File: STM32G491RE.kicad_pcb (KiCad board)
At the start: 2 copper layers, 210.5 x 121.5 mm, 147 parts, among them J4 OLED I2C, J5 BAT VIN, J6 TYPE-C_16PIN_2MD__073_, J7 Battery, Q1 PMOS, Q2 PMOS, Q3 PMOS, U1 TPS564257DRLR, U10 ESP32-S3-MINI-1-N8, U2 STM32G491RETx, U3 TPS2113ADRBR, U4 DRV8835DSSR, U5 M24M02-DRMN6TP, U6 MP2639A, U7 TPS79601DRBR, U8 LMV331M5, U9 LMV331M5, Y1 24MHz, Y2 32.768KHz

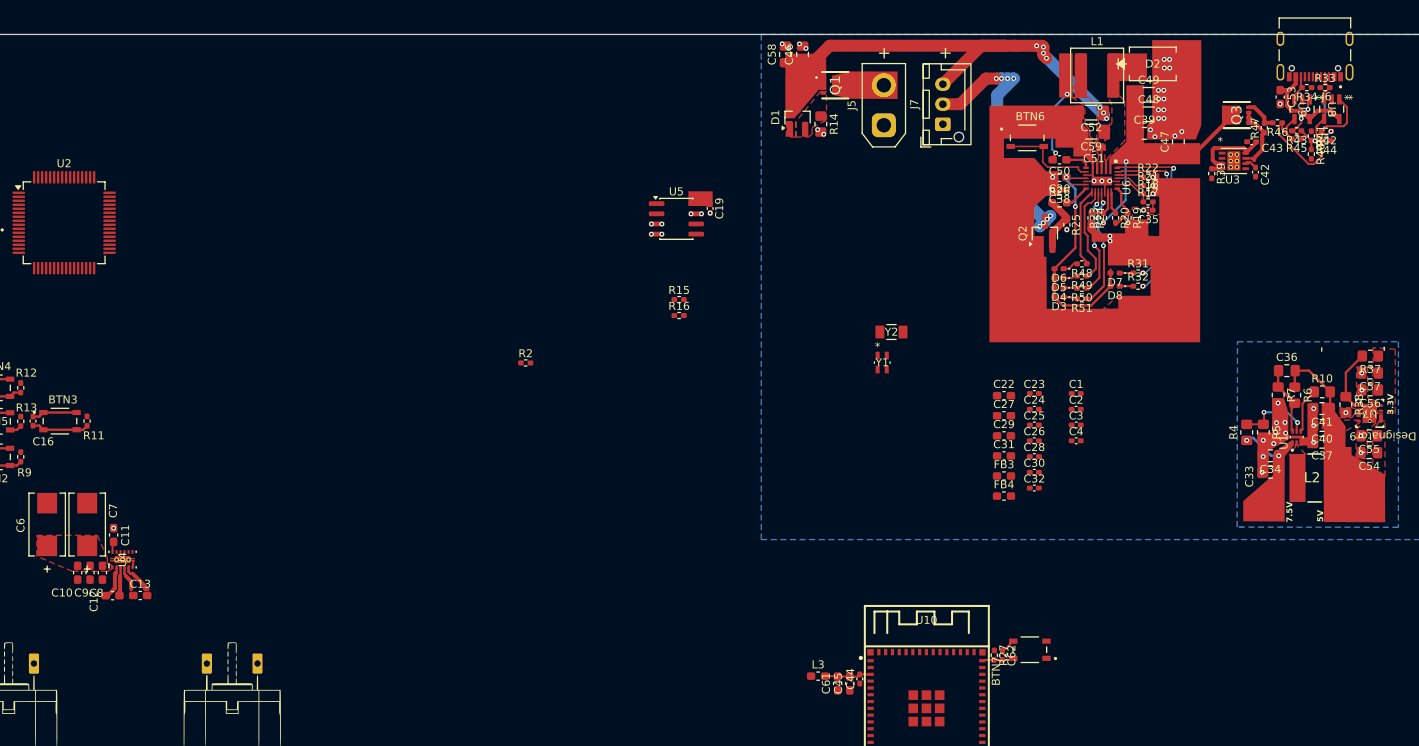
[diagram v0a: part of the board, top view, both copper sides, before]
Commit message: changed most of the components to 0805
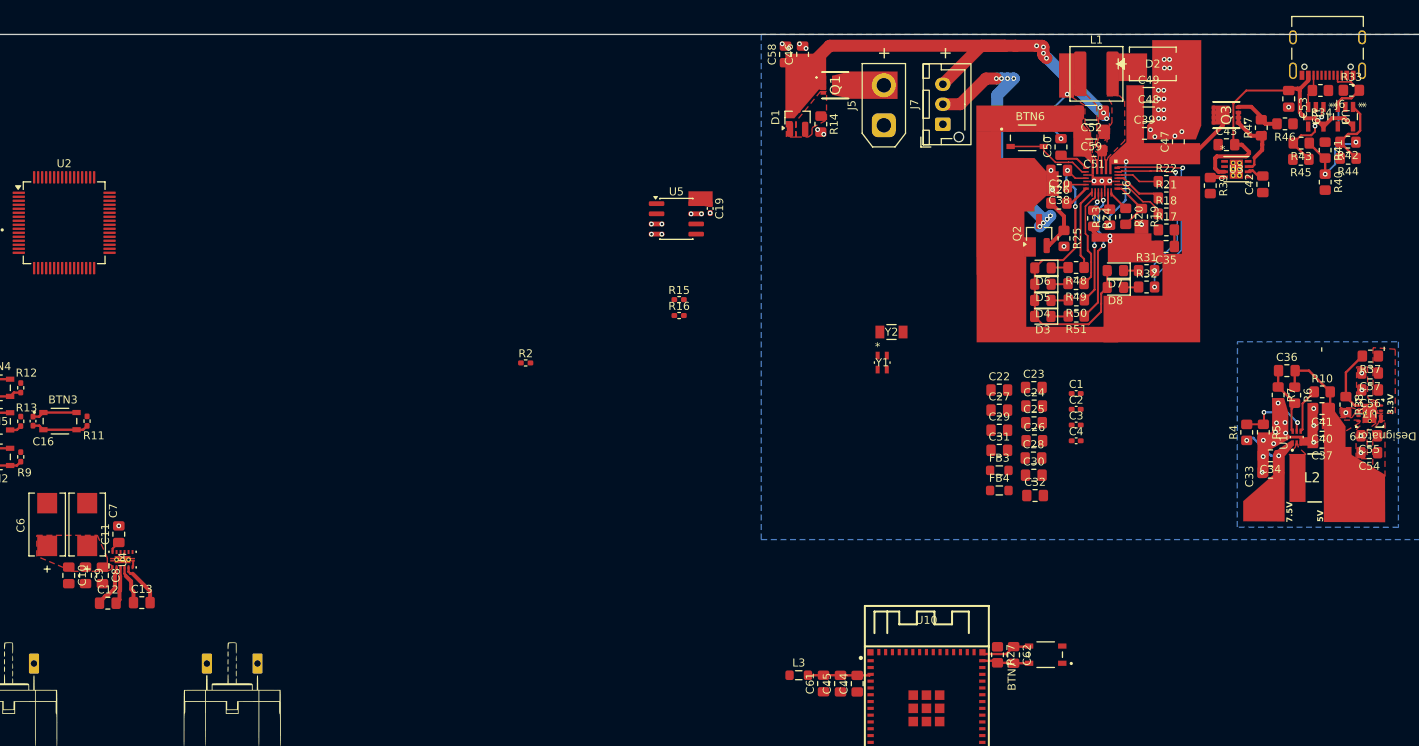
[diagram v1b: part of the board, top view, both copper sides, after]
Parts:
- C10, C11, C12, C13, C20, C22, C27, C29, C31, C45, C50, C51, C53, C61, C8, C9: footprint Capacitor_SMD:C_0603_1608Metric_Pad1.08x0.95mm_HandSolder -> Capacitor_SMD:C_0805_2012Metric_Pad1.18x1.45mm_HandSolder
- C23, C24, C25, C26, C28, C30, C32, C35, C38, C42, C43, C44, C62: footprint Capacitor_SMD:C_0402_1005Metric_Pad0.74x0.62mm_HandSolder -> Capacitor_SMD:C_0805_2012Metric_Pad1.18x1.45mm_HandSolder
- D3, D4, D5, D6, D7, D8: footprint LED_SMD:LED_0402_1005Metric_Pad0.77x0.64mm_HandSolder -> LED_SMD:LED_0805_2012Metric_Pad1.15x1.40mm_HandSolder
- FB3, FB4, L3: footprint Inductor_SMD:L_0603_1608Metric_Pad1.05x0.95mm_HandSolder -> Inductor_SMD:L_0805_2012Metric_Pad1.05x1.20mm_HandSolder
- R17, R18, R19, R20, R21, R22, R23, R24, R25, R27, R31, R32, R33, R34, R39, R40, R41, R42, R43, R44, R45, R46, R47, R48, R49, R50, R51: footprint Resistor_SMD:R_0402_1005Metric_Pad0.72x0.64mm_HandSolder -> Resistor_SMD:R_0805_2012Metric_Pad1.20x1.40mm_HandSolder
- R26: footprint Resistor_SMD:R_0603_1608Metric_Pad0.98x0.95mm_HandSolder -> Resistor_SMD:R_0805_2012Metric_Pad1.20x1.40mm_HandSolder
- moved C35 5.06 mm to (192.7, 39.9)
- moved R17 4.18 mm to (192.8, 37.9)
- moved R40 3.91 mm to (212.6, 31.9)
- moved R44 3.50 mm to (215.5, 28.9)
- moved R18 3.40 mm to (192.8, 35.9)
- moved R33 3.31 mm to (215.9, 20.4)
- moved C43 3.17 mm to (200.3, 27.2)
- moved D3 3.16 mm to (177.3, 48.7)
- moved R42 3.03 mm to (215.5, 26.9)
- moved R21 2.75 mm to (192.8, 33.9)
- moved R45 2.62 mm to (209.6, 29.0)
- moved D4 2.57 mm to (177.3, 46.7)
- moved R41 2.47 mm to (212.6, 27.9)
- moved L3 2.42 mm to (146.8, 93.5)
- moved R22 2.34 mm to (192.8, 31.8)
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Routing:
- net Net-(R44-Pad2): track 19.9 -> 0.00 mm
- net +5V_USBC: track 22.6 -> 36.7 mm
- net +VCC: track 29.5 -> 40.4 mm
- net +VREF_COMP: track 7.01 -> 12.6 mm
- net CC1: track 3.38 -> 7.85 mm
- net GND: track 5.02 -> 8.87 mm, vias 61 -> 57
- net Net-(R43-Pad2): track 6.57 -> 9.64 mm
- net Net-(U6-SW): track 12.4 -> 9.84 mm
- net Net-(U6-ISET): track 3.65 -> 6.16 mm
- net Net-(U6-LED4): track 15.1 -> 17.5 mm
- net Net-(U6-IB): track 4.76 -> 6.94 mm
- net Net-(U10-3V3): track 5.82 -> 7.90 mm
- net Net-(U6-ILIM): track 3.48 -> 5.48 mm
- net ESP_EN: track 3.99 -> 5.98 mm
- net BOUT1: track 3.08 -> 4.89 mm
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
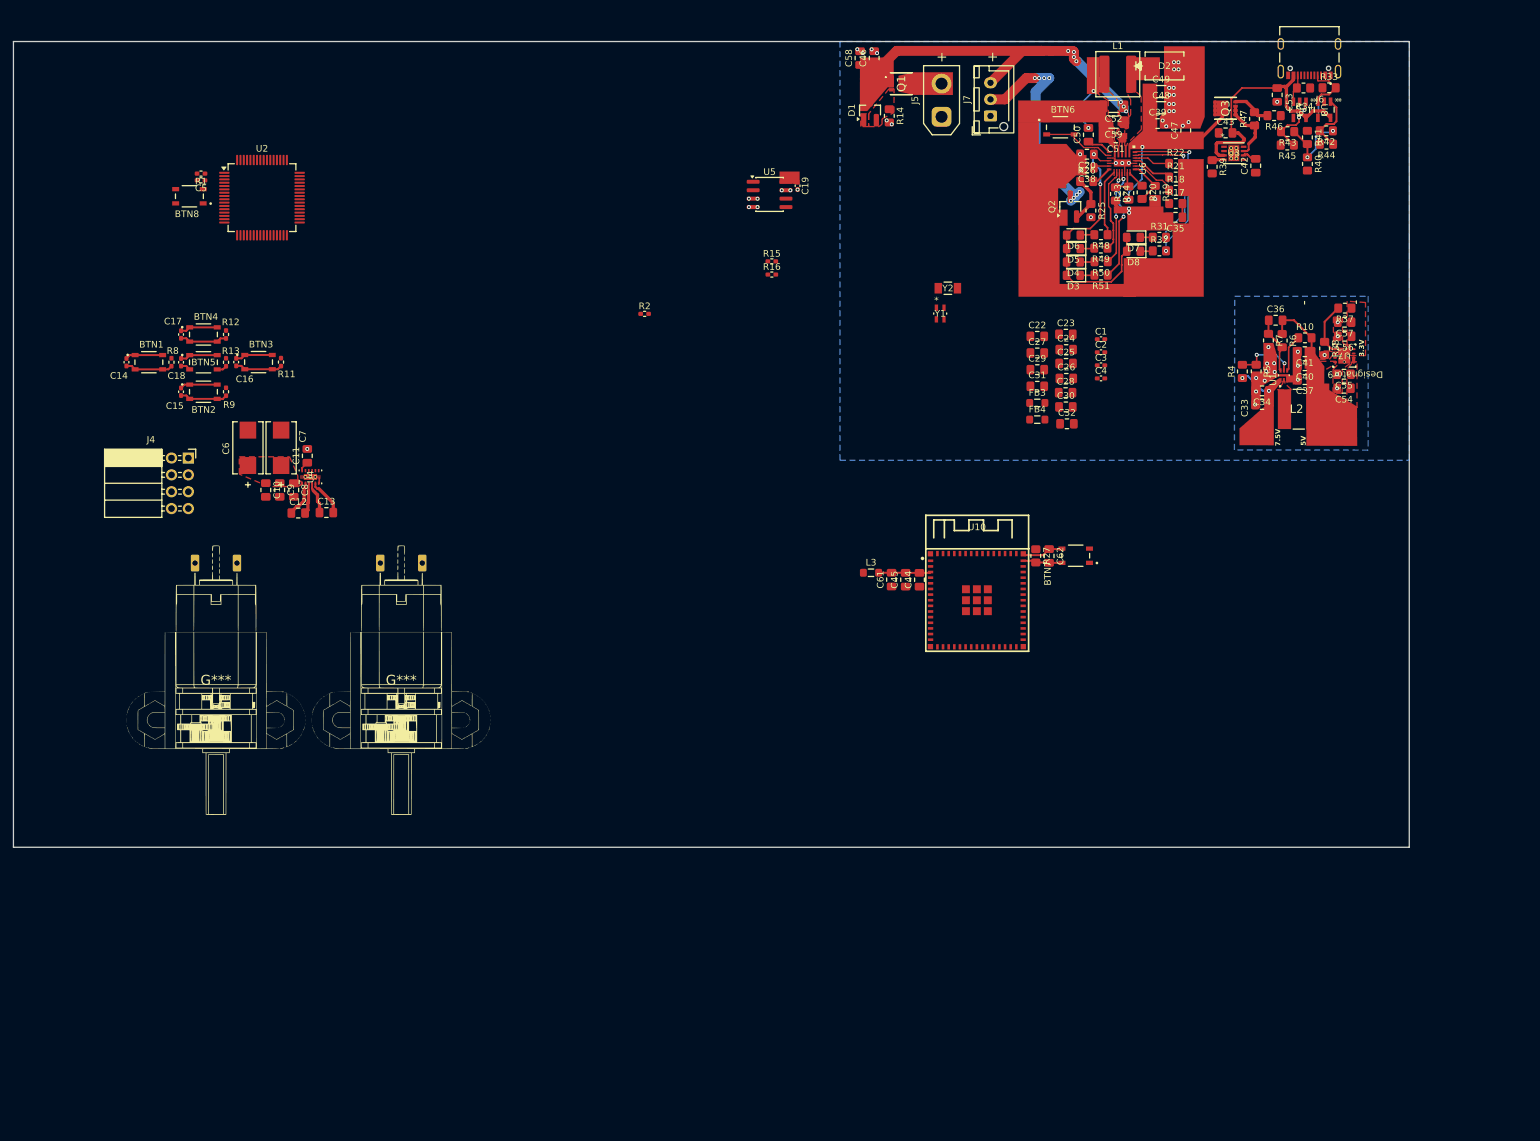
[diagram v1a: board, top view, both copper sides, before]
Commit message: finalized parts before sensors
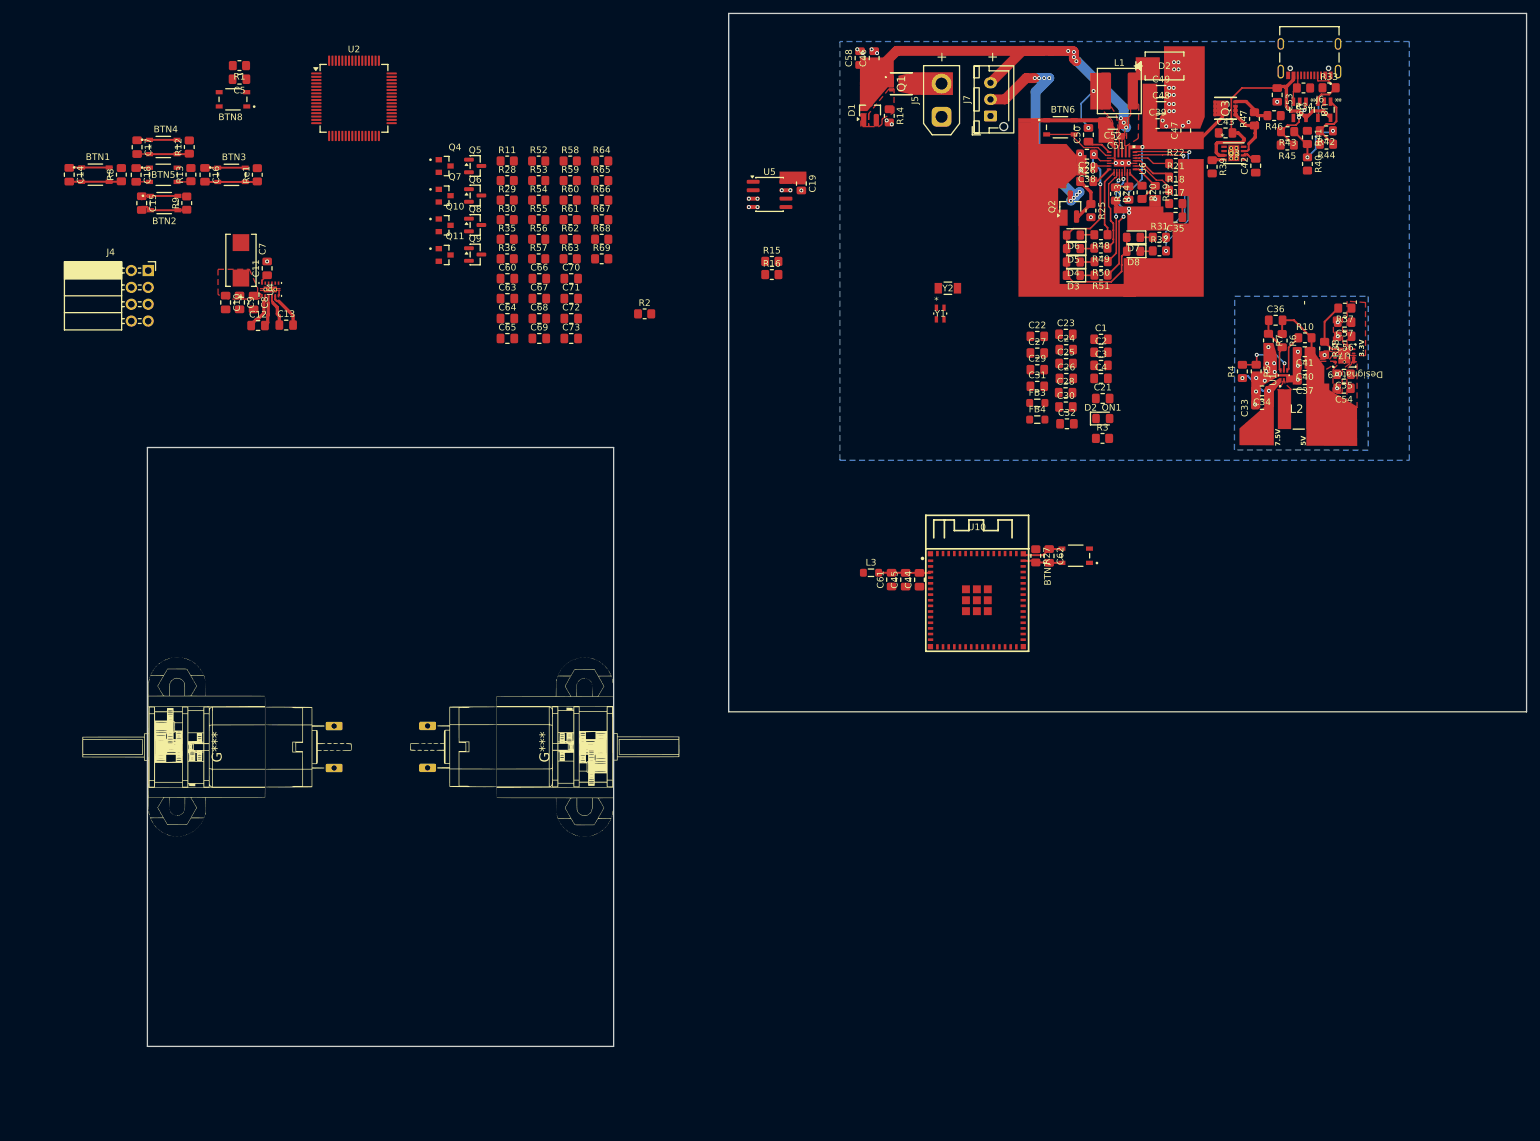
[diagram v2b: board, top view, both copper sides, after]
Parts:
- removed C59: 22uF, Capacitor_SMD:C_1206_3216Metric_Pad1.33x1.80mm_HandSolder
- removed C6: 220uF, kicad_custom:CAPMP7.6X4.3_3.1N_KEM
- added C21: 100nF, Capacitor_SMD:C_0805_2012Metric_Pad1.18x1.45mm_HandSolder, F.Cu at (181.7, 67.3)
- added C60: 22uF, Capacitor_SMD:C_0805_2012Metric_Pad1.18x1.45mm_HandSolder, F.Cu at (92.0, 49.2)
- added C63: 22uF, Capacitor_SMD:C_0805_2012Metric_Pad1.18x1.45mm_HandSolder, F.Cu at (92.0, 52.2)
- added C64: 100pF, Capacitor_SMD:C_0805_2012Metric_Pad1.18x1.45mm_HandSolder, F.Cu at (92.0, 55.2)
- added C65: 100pF, Capacitor_SMD:C_0805_2012Metric_Pad1.18x1.45mm_HandSolder, F.Cu at (92.0, 58.2)
- added C66: 22uF, Capacitor_SMD:C_0805_2012Metric_Pad1.18x1.45mm_HandSolder, F.Cu at (96.8, 49.2)
- added C67: 22uF, Capacitor_SMD:C_0805_2012Metric_Pad1.18x1.45mm_HandSolder, F.Cu at (96.8, 52.2)
- added C68: 100pF, Capacitor_SMD:C_0805_2012Metric_Pad1.18x1.45mm_HandSolder, F.Cu at (96.8, 55.2)
- added C69: 100pF, Capacitor_SMD:C_0805_2012Metric_Pad1.18x1.45mm_HandSolder, F.Cu at (96.8, 58.2)
- added C70: 22uF, Capacitor_SMD:C_0805_2012Metric_Pad1.18x1.45mm_HandSolder, F.Cu at (101.6, 49.2)
- added C71: 22uF, Capacitor_SMD:C_0805_2012Metric_Pad1.18x1.45mm_HandSolder, F.Cu at (101.6, 52.2)
- added C72: 22uF, Capacitor_SMD:C_0805_2012Metric_Pad1.18x1.45mm_HandSolder, F.Cu at (101.6, 55.2)
- added C73: 22uF, Capacitor_SMD:C_0805_2012Metric_Pad1.18x1.45mm_HandSolder, F.Cu at (101.6, 58.2)
- added D2_ON1: LED, LED_SMD:LED_0805_2012Metric_Pad1.15x1.40mm_HandSolder, F.Cu at (181.8, 70.3)
- added Q10: IBLML6344, kicad_custom:TRANS_IRLML6344TRPBF, F.Cu at (82.5, 41.1)
- added Q11: IBLML6344, kicad_custom:TRANS_IRLML6344TRPBF, F.Cu at (82.5, 45.6)
- added Q4: IBLML6344, kicad_custom:TRANS_IRLML6344TRPBF, F.Cu at (82.5, 32.2)
- added Q5: BC817-40, Package_TO_SOT_SMD:SOT-23, F.Cu at (87.1, 32.2)
- added Q6: BC817-40, Package_TO_SOT_SMD:SOT-23, F.Cu at (87.1, 36.6)
- added Q7: IBLML6344, kicad_custom:TRANS_IRLML6344TRPBF, F.Cu at (82.5, 36.7)
- added Q8: BC817-40, Package_TO_SOT_SMD:SOT-23, F.Cu at (87.1, 41.1)
- added Q9: BC817-40, Package_TO_SOT_SMD:SOT-23, F.Cu at (87.1, 45.5)
- added R11: 2k, Resistor_SMD:R_0805_2012Metric_Pad1.20x1.40mm_HandSolder, F.Cu at (92.0, 31.4)
- added R28: 10k, Resistor_SMD:R_0805_2012Metric_Pad1.20x1.40mm_HandSolder, F.Cu at (92.0, 34.4)
- added R29: 100, Resistor_SMD:R_0805_2012Metric_Pad1.20x1.40mm_HandSolder, F.Cu at (92.0, 37.4)
- added R3: 510, Resistor_SMD:R_0805_2012Metric_Pad1.20x1.40mm_HandSolder, F.Cu at (181.7, 73.3)
- added R30: 0.56, Resistor_SMD:R_0805_2012Metric_Pad1.20x1.40mm_HandSolder, F.Cu at (92.0, 40.3)
- added R35: 100k, Resistor_SMD:R_0805_2012Metric_Pad1.20x1.40mm_HandSolder, F.Cu at (92.0, 43.2)
- added R36: 1k, Resistor_SMD:R_0805_2012Metric_Pad1.20x1.40mm_HandSolder, F.Cu at (92.0, 46.2)
- added R52: 1k, Resistor_SMD:R_0805_2012Metric_Pad1.20x1.40mm_HandSolder, F.Cu at (96.7, 31.4)
- added R53: 100k, Resistor_SMD:R_0805_2012Metric_Pad1.20x1.40mm_HandSolder, F.Cu at (96.7, 34.4)
- added R54: 100, Resistor_SMD:R_0805_2012Metric_Pad1.20x1.40mm_HandSolder, F.Cu at (96.7, 37.4)
- added R55: 0.56, Resistor_SMD:R_0805_2012Metric_Pad1.20x1.40mm_HandSolder, F.Cu at (96.7, 40.3)
- added R56: 2k, Resistor_SMD:R_0805_2012Metric_Pad1.20x1.40mm_HandSolder, F.Cu at (96.7, 43.2)
- added R57: 10k, Resistor_SMD:R_0805_2012Metric_Pad1.20x1.40mm_HandSolder, F.Cu at (96.7, 46.2)
- added R58: 1k, Resistor_SMD:R_0805_2012Metric_Pad1.20x1.40mm_HandSolder, F.Cu at (101.5, 31.4)
- added R59: 1k, Resistor_SMD:R_0805_2012Metric_Pad1.20x1.40mm_HandSolder, F.Cu at (101.5, 34.4)
- added R60: 100k, Resistor_SMD:R_0805_2012Metric_Pad1.20x1.40mm_HandSolder, F.Cu at (101.5, 37.4)
- added R61: 100k, Resistor_SMD:R_0805_2012Metric_Pad1.20x1.40mm_HandSolder, F.Cu at (101.5, 40.3)
- added R62: 100, Resistor_SMD:R_0805_2012Metric_Pad1.20x1.40mm_HandSolder, F.Cu at (101.5, 43.2)
- added R63: 0.56, Resistor_SMD:R_0805_2012Metric_Pad1.20x1.40mm_HandSolder, F.Cu at (101.5, 46.2)
- added R64: 100, Resistor_SMD:R_0805_2012Metric_Pad1.20x1.40mm_HandSolder, F.Cu at (106.2, 31.4)
- added R65: 0.56, Resistor_SMD:R_0805_2012Metric_Pad1.20x1.40mm_HandSolder, F.Cu at (106.2, 34.4)
- added R66: 2k, Resistor_SMD:R_0805_2012Metric_Pad1.20x1.40mm_HandSolder, F.Cu at (106.2, 37.4)
- added R67: 2k, Resistor_SMD:R_0805_2012Metric_Pad1.20x1.40mm_HandSolder, F.Cu at (106.2, 40.3)
- added R68: 10k, Resistor_SMD:R_0805_2012Metric_Pad1.20x1.40mm_HandSolder, F.Cu at (106.2, 43.2)
- added R69: 10k, Resistor_SMD:R_0805_2012Metric_Pad1.20x1.40mm_HandSolder, F.Cu at (106.2, 46.2)
- C1, C14, C15, C16, C17, C18, C19, C2, C3, C4: footprint Capacitor_SMD:C_0402_1005Metric_Pad0.74x0.62mm_HandSolder -> Capacitor_SMD:C_0805_2012Metric_Pad1.18x1.45mm_HandSolder
- C5: footprint Resistor_SMD:R_0402_1005Metric_Pad0.72x0.64mm_HandSolder -> Capacitor_SMD:C_0805_2012Metric_Pad1.18x1.45mm_HandSolder
- C51: footprint Capacitor_SMD:C_0805_2012Metric_Pad1.18x1.45mm_HandSolder -> Capacitor_SMD:C_0603_1608Metric_Pad1.08x0.95mm_HandSolder
- R1, R12, R13, R15, R16, R2, R8, R9: footprint Resistor_SMD:R_0402_1005Metric_Pad0.72x0.64mm_HandSolder -> Resistor_SMD:R_0805_2012Metric_Pad1.20x1.40mm_HandSolder
- Re1: renamed from R11; footprint Resistor_SMD:R_0402_1005Metric_Pad0.72x0.64mm_HandSolder -> Resistor_SMD:R_0805_2012Metric_Pad1.20x1.40mm_HandSolder
- moved C14 29.6 mm to (25.9, 33.5)
- moved BTN1 29.4 mm to (29.9, 33.5)
- moved R8 29.3 mm to (33.8, 33.5)
- moved BTN2 29.1 mm to (40.2, 37.8)
- moved C15 29.1 mm to (36.8, 37.8)
- moved R9 29.1 mm to (43.6, 37.8)
- moved C18 29.1 mm to (36.0, 33.5)
- moved C17 29.0 mm to (36.1, 29.4)
- moved BTN5 28.9 mm to (40.1, 33.5)
- moved C10 28.9 mm to (49.5, 52.8)
- moved C11 28.9 mm to (55.8, 47.6)
- moved C12 28.9 mm to (54.4, 56.3)
- moved C7 28.9 mm to (51.8, 46.4)
- moved C8 28.9 mm to (53.7, 52.8)
- moved C9 28.9 mm to (51.6, 52.8)
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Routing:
- net VM: track 61.8 -> 64.9 mm
- net VCC: track 29.8 -> 27.4 mm
- net BTN5: track 3.04 -> 4.15 mm
- net BTN3: track 7.16 -> 7.94 mm
- net BTN4: track 7.19 -> 7.90 mm
- net BTN1: track 7.19 -> 7.90 mm
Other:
- board size 210.5 x 121.5 mm -> 207.9 x 155.8 mm

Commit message: fixed sensor schematic and begun pcb layout
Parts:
- added D10: Transmitter, Connector_PinHeader_2.54mm:PinHeader_1x02_P2.54mm_Vertical, F.Cu at (88.4, 23.1)
- added D11: Transmitter, Connector_PinHeader_2.54mm:PinHeader_1x02_P2.54mm_Vertical, F.Cu at (93.0, 23.1)
- added D12: Receiver, Connector_PinHeader_2.54mm:PinHeader_1x02_P2.54mm_Vertical, F.Cu at (97.6, 23.1)
- added D13: Transmitter, Connector_PinHeader_2.54mm:PinHeader_1x02_P2.54mm_Vertical, F.Cu at (102.2, 23.1)
- added D14: Transmitter, Connector_PinHeader_2.54mm:PinHeader_1x02_P2.54mm_Vertical, F.Cu at (106.7, 23.1)
- added D15: Receiver, Connector_PinHeader_2.54mm:PinHeader_1x02_P2.54mm_Vertical, F.Cu at (111.3, 23.1)
- added D16: Receiver, Connector_PinHeader_2.54mm:PinHeader_1x02_P2.54mm_Vertical, F.Cu at (115.9, 23.1)
- added D9: Receiver, Connector_PinHeader_2.54mm:PinHeader_1x02_P2.54mm_Vertical, F.Cu at (83.8, 23.1)
- added R70: 180k, Resistor_SMD:R_0805_2012Metric_Pad1.20x1.40mm_HandSolder, F.Cu at (176.6, 18.7)
- added R71: 100k, Resistor_SMD:R_0805_2012Metric_Pad1.20x1.40mm_HandSolder, F.Cu at (176.6, 21.6)
- moved C14 141.7 mm to (98.8, 155.1), turned to 90 degrees
- moved BTN1 137.9 mm to (94.8, 155.1), turned to 180 degrees
- moved R8 134.4 mm to (90.9, 155.1), turned to -90 degrees
- moved C17 134.2 mm to (90.7, 151.9), turned to 0 degrees
- moved C18 132.3 mm to (94.8, 152.1), turned to 0 degrees
- moved C15 130.0 mm to (99.0, 152.0), turned to 0 degrees
- moved BTN4 129.0 mm to (90.6, 148.0), turned to 90 degrees
- moved BTN5 126.9 mm to (94.8, 148.0), turned to 90 degrees
- moved BTN2 124.9 mm to (99.0, 148.0), turned to 90 degrees
- moved R12 123.8 mm to (90.6, 144.1), turned to 180 degrees
- moved R13 121.4 mm to (94.8, 143.8), turned to 180 degrees
- moved R9 119.7 mm to (99.0, 143.9), turned to 180 degrees
- moved C16 119.3 mm to (98.7, 140.8), turned to 90 degrees
- moved BTN3 116.0 mm to (94.7, 140.8), turned to 180 degrees
- moved Re1 113.3 mm to (90.8, 140.8), turned to -90 degrees
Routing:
- net VCC: track 27.4 -> 56.6 mm
- net BTN5: track 4.15 -> 8.30 mm
- net BATT_LEVEL: track 0.00 -> 3.78 mm
- net VM: track 64.9 -> 68.3 mm
- net BTN2: track 7.19 -> 6.24 mm
- net GND: vias 57 -> 58
